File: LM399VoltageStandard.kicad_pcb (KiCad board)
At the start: 2 copper layers, 31 parts, among them J1 Screw_Terminal_01x04, U1 LM399, U2 LT1001, U3 LT3045xDD, U5 LM7815

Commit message: Started PCB
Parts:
- removed D5: 1N4148, Diode_THT:D_DO-35_SOD27_P7.62mm_Horizontal
- added C20: 100n, Capacitor_SMD:C_0603_1608Metric, F.Cu at (143.8, 61.4)
- added C21: 1n, Capacitor_SMD:C_0603_1608Metric, F.Cu at (106.6, 65.1)
- added C22: 10u, Capacitor_Tantalum_SMD:CP_EIA-7132-20_AVX-U, F.Cu at (140.8, 64.2)
- added JP10: Jumper_2_Open, Jumper:SolderJumper-2_P1.3mm_Open_RoundedPad1.0x1.5mm, F.Cu at (124.9, 59.1)
- added JP11: Jumper_2_Open, Jumper:SolderJumper-2_P1.3mm_Open_RoundedPad1.0x1.5mm, F.Cu at (127.4, 59.1)
- added JP12: Jumper_2_Open, Jumper:SolderJumper-2_P1.3mm_Open_RoundedPad1.0x1.5mm, F.Cu at (129.9, 59.1)
- added JP13: Jumper_2_Open, Jumper:SolderJumper-2_P1.3mm_Open_RoundedPad1.0x1.5mm, F.Cu at (132.4, 59.1)
- added JP14: Jumper_2_Open, Jumper:SolderJumper-2_P1.3mm_Open_RoundedPad1.0x1.5mm, F.Cu at (134.9, 59.1)
- added JP8: Jumper_2_Open, Jumper:SolderJumper-2_P1.3mm_Open_RoundedPad1.0x1.5mm, F.Cu at (119.9, 59.1)
- added JP9: Jumper_2_Open, Jumper:SolderJumper-2_P1.3mm_Open_RoundedPad1.0x1.5mm, F.Cu at (122.4, 59.1)
- added R1: 8k06, Resistor_SMD:R_0603_1608Metric, F.Cu at (104.6, 65.0)
- added R10: 8M25, Resistor_THT:R_Axial_DIN0204_L3.6mm_D1.6mm_P7.62mm_Horizontal, F.Cu at (130.1, 61.9)
- added R11: 35k7, Resistor_SMD:R_0603_1608Metric, F.Cu at (117.4, 63.2)
- added R12: 8M25, Resistor_THT:R_Axial_DIN0204_L3.6mm_D1.6mm_P7.62mm_Horizontal, F.Cu at (132.5, 61.9)
- added R13: 511k, Resistor_SMD:R_0603_1608Metric, F.Cu at (119.9, 62.7)
- added R14: 8M25, Resistor_THT:R_Axial_DIN0204_L3.6mm_D1.6mm_P7.62mm_Horizontal, F.Cu at (132.5, 71.9)
- added R15: 32M, Resistor_THT:R_Axial_DIN0207_L6.3mm_D2.5mm_P10.16mm_Horizontal, F.Cu at (135.4, 61.9)
- added R16: 32M, Resistor_SMD:R_0805_2012Metric, F.Cu at (135.4, 65.7)
- added R17: 50R, Resistor_SMD:R_0805_2012Metric, F.Cu at (138.1, 58.4)
- added R4: 5k, LM399VoltageStandard:ZFoilResistor, F.Cu at (114.5, 54.7)
- added R5: 10k, Resistor_THT:R_Axial_DIN0207_L6.3mm_D2.5mm_P10.16mm_Horizontal, F.Cu at (114.5, 61.9)
- added R6: 2k, Resistor_SMD:R_1206_3216Metric, F.Cu at (117.4, 59.2)
- added R7: 1M02, Resistor_SMD:R_0805_2012Metric, F.Cu at (122.4, 62.8)
- added R8: 2M05, Resistor_SMD:R_0805_2012Metric, F.Cu at (124.9, 62.9)
- added R9: 4M12, Resistor_THT:R_Axial_DIN0207_L6.3mm_D2.5mm_P10.16mm_Horizontal, F.Cu at (127.5, 66.3)
- added U4: 7818, Package_TO_SOT_SMD:TO-263-2, F.Cu at (249.8, 117.5)
- moved U1 117.0 mm to (104.4, 72.8), turned to 180 degrees
- moved C6 113.8 mm to (102.9, 65.1), turned to -90 degrees
- moved U2 113.0 mm to (110.4, 63.5), turned to 90 degrees
- moved C1 110.0 mm to (108.9, 59.0), turned to 180 degrees
- moved U5 68.9 mm to (247.7, 100.0)
- moved R3 57.0 mm to (249.1, 128.9)
- moved D6 55.2 mm to (235.3, 108.8)
- moved C14 55.2 mm to (234.8, 121.1)
- moved C9 55.2 mm to (234.8, 114.6)
- moved C18 55.2 mm to (234.8, 127.7)
- moved C10 51.6 mm to (241.1, 139.0)
- moved C7 51.6 mm to (241.1, 134.0)
- moved C8 51.6 mm to (241.1, 136.5)
- moved C2 51.4 mm to (241.1, 131.5)
- moved C11 51.4 mm to (245.1, 128.9)
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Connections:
- C12 pad 2: Masa -> GND_H
- C13 pad 2: Masa -> GND_H
- C14 pad 2: Masa -> GND_H
- C15 pad 2: Masa -> GND_H
- C16 pad 2: Masa -> GND_H
- D6 pad 1: Masa -> GND_H
- U1 pad 4: Masa -> GND_H
- U2 pad 6: /10V -> Net-(JP10-B)
- U5 pad 2: Masa -> GND_H
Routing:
- net Net-(U2--): track 0.00 -> 49.8 mm
- net Net-(JP10-B): track 0.00 -> 28.4 mm
- net Net-(U2-+): track 0.00 -> 16.9 mm
- net Masa: track 0.00 -> 12.6 mm, vias 0 -> 7
- net /10V: track 0.00 -> 7.32 mm
- net Net-(JP11-A): track 0.00 -> 6.57 mm
- net +15V: track 0.00 -> 5.34 mm, vias 0 -> 1
- net Net-(JP14-A): track 0.00 -> 5.19 mm
- net Net-(R12-Pad2): track 0.00 -> 2.47 mm
- net Net-(JP10-A): track 0.00 -> 2.18 mm
- net Net-(JP12-A): track 0.00 -> 2.15 mm
- net Net-(JP9-A): track 0.00 -> 2.12 mm
- net Net-(JP8-A): track 0.00 -> 2.12 mm
- net Net-(JP13-A): track 0.00 -> 2.12 mm
- added copper zone on In1.Cu, net Masa
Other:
- board outline added: 100 x 80 mm
- copper layers 2 -> 4

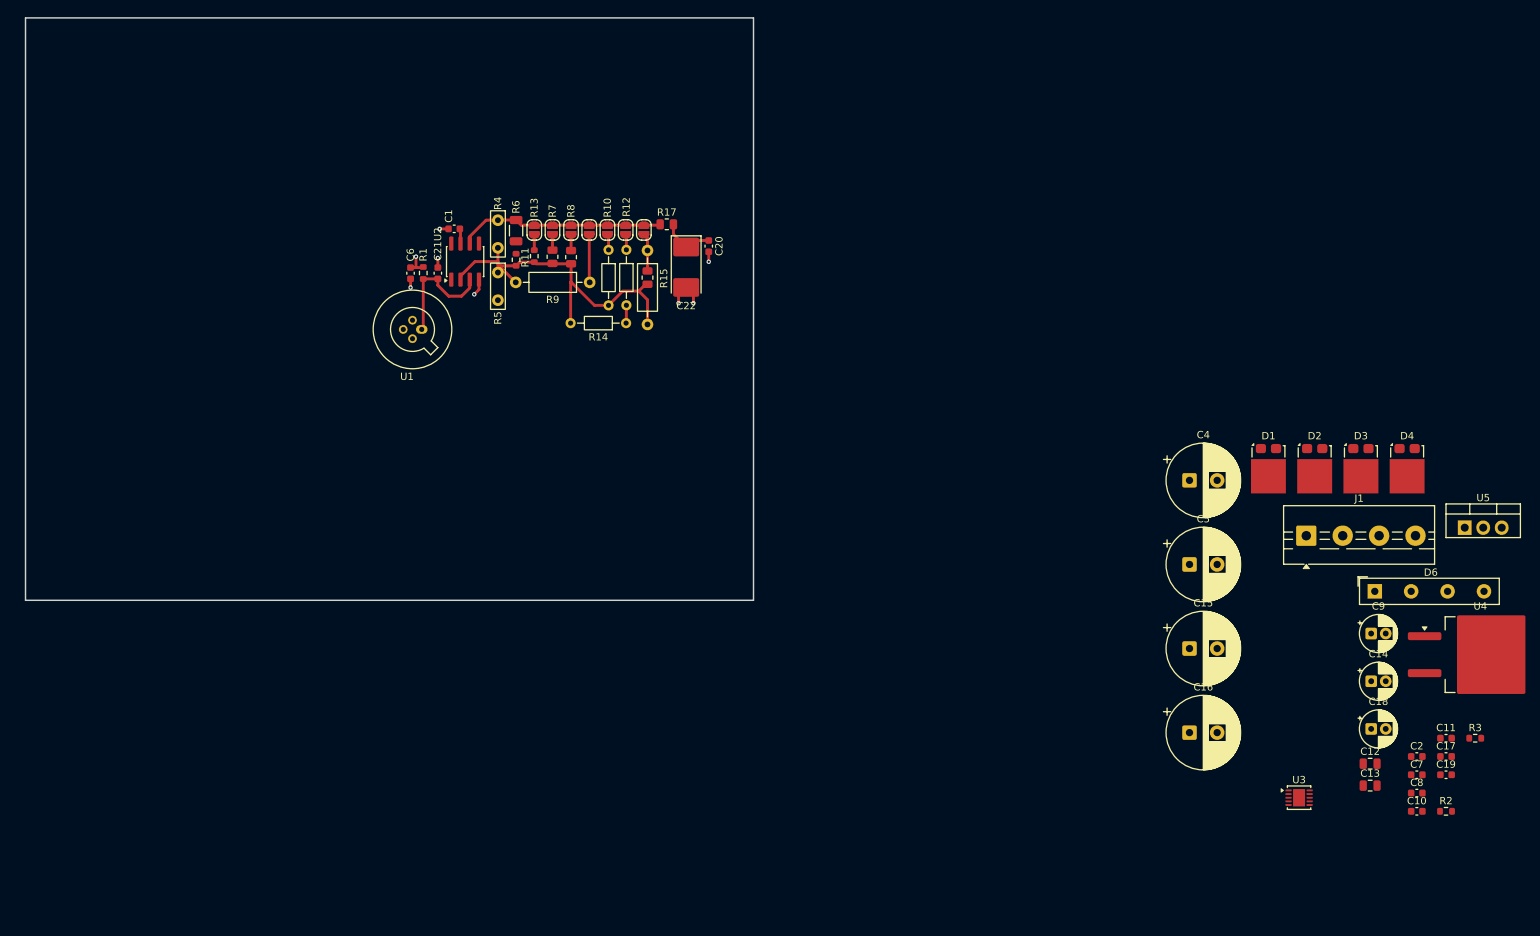
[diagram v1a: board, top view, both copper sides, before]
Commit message: Added MCU
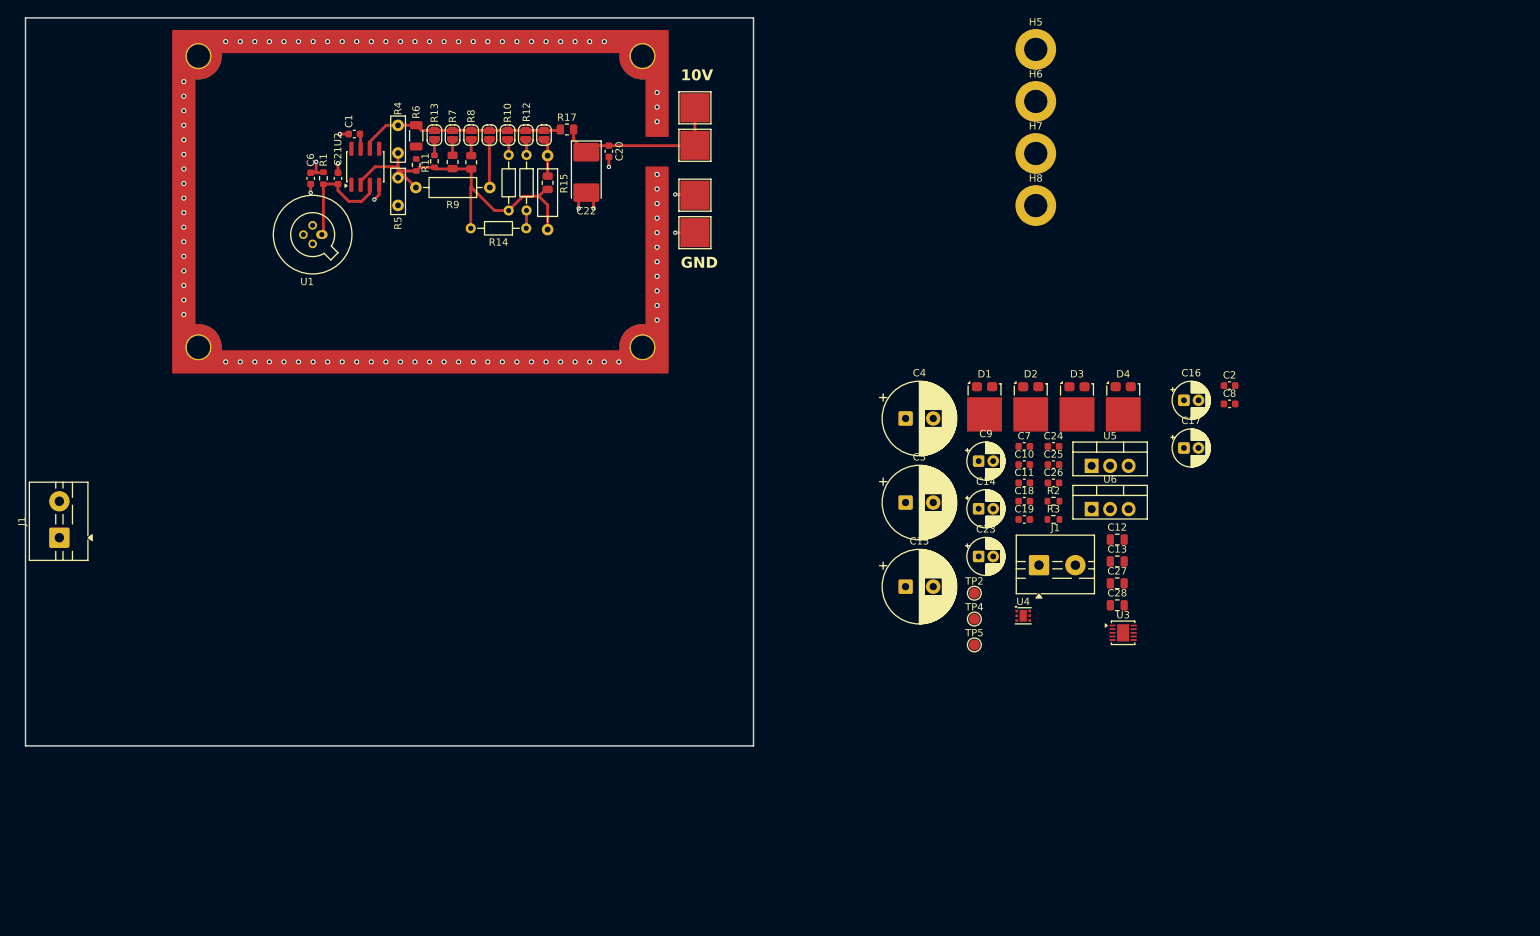
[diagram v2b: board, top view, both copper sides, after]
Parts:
- removed D6: KBP10, Diode_THT:Diode_Bridge_19.0x3.5x10.0mm_P5.0mm
- removed the J1 at (225.9, 101.1)
- added C23: 47u, Capacitor_THT:CP_Radial_D5.0mm_P2.00mm, F.Cu at (180.9, 104.0)
- added C24: 100n, Capacitor_SMD:C_0603_1608Metric, F.Cu at (191.2, 88.9)
- added C25: 100n, Capacitor_SMD:C_0603_1608Metric, F.Cu at (191.2, 91.4)
- added C26: 100n, Capacitor_SMD:C_0603_1608Metric, F.Cu at (191.2, 93.9)
- added C27: 10u, Capacitor_SMD:C_0805_2012Metric, F.Cu at (200.0, 107.7)
- added C28: 10u, Capacitor_SMD:C_0805_2012Metric, F.Cu at (200.0, 110.7)
- added H1: MountingHole_Pad, MountingHole:MountingHole_3.2mm_M3_Pad_TopBottom, F.Cu at (134.8, 75.2)
- added H2: MountingHole_Pad, MountingHole:MountingHole_3.2mm_M3_Pad_TopBottom, F.Cu at (73.8, 75.2)
- added H3: MountingHole_Pad, MountingHole:MountingHole_3.2mm_M3_Pad_TopBottom, F.Cu at (73.8, 35.2)
- added H4: MountingHole_Pad, MountingHole:MountingHole_3.2mm_M3_Pad_TopBottom, F.Cu at (134.8, 35.2)
- added H5: MountingHole, MountingHole:MountingHole_3.2mm_M3_DIN965_Pad, F.Cu at (188.8, 34.3)
- added H6: MountingHole, MountingHole:MountingHole_3.2mm_M3_DIN965_Pad, F.Cu at (188.8, 41.5)
- added H7: MountingHole, MountingHole:MountingHole_3.2mm_M3_DIN965_Pad, F.Cu at (188.8, 48.6)
- added H8: MountingHole, MountingHole:MountingHole_3.2mm_M3_DIN965_Pad, F.Cu at (188.8, 55.8)
- added J1: Screw_Terminal_01x02, TerminalBlock:TerminalBlock_MaiXu_MX126-5.0-02P_1x02_P5.00mm, F.Cu at (189.2, 105.2)
- added J1: Screw_Terminal_01x02, TerminalBlock:TerminalBlock_MaiXu_MX126-5.0-02P_1x02_P5.00mm, F.Cu at (54.6, 101.4)
- added TP2: TestPoint, TestPoint:TestPoint_Pad_D1.5mm, F.Cu at (180.3, 109.0)
- added TP3: TestPoint, TestPoint:TestPoint_Pad_4.0x4.0mm, F.Cu at (141.9, 47.5)
- added TP4: TestPoint, TestPoint:TestPoint_Pad_D1.5mm, F.Cu at (180.3, 112.6)
- added TP5: TestPoint, TestPoint:TestPoint_Pad_D1.5mm, F.Cu at (180.3, 116.1)
- added TP6: TestPoint, TestPoint:TestPoint_Pad_4.0x4.0mm, F.Cu at (141.9, 54.4)
- added TP7: TestPoint, TestPoint:TestPoint_Pad_4.0x4.0mm, F.Cu at (141.9, 42.4)
- added TP8: TestPoint, TestPoint:TestPoint_Pad_4.0x4.0mm, F.Cu at (141.9, 59.5)
- added U6: LM7805_TO220, Package_TO_SOT_THT:TO-220-3_Vertical, F.Cu at (196.4, 97.5)
- C16: value 1000u -> 47u; footprint Capacitor_THT:CP_Radial_D10.0mm_P3.80mm -> Capacitor_THT:CP_Radial_D5.0mm_P2.00mm
- C17: value 100n -> 47u; footprint Capacitor_SMD:C_0603_1608Metric -> Capacitor_THT:CP_Radial_D5.0mm_P2.00mm
- C18: value 47u -> 100n; footprint Capacitor_THT:CP_Radial_D5.0mm_P2.00mm -> Capacitor_SMD:C_0603_1608Metric
- U4: value 7818 -> TLV75533PDRV; footprint Package_TO_SOT_SMD:TO-263-2 -> Package_SON:WSON-6-1EP_2x2mm_P0.65mm_EP1x1.6mm
- moved C10 71.9 mm to (187.2, 91.4)
- moved C7 70.3 mm to (187.2, 88.9)
- moved R2 68.7 mm to (191.2, 96.4)
- moved C11 67.7 mm to (187.2, 93.9)
- moved C19 67.7 mm to (187.2, 98.9)
- moved R3 65.3 mm to (191.2, 98.9)
- moved U4 63.0 mm to (187.0, 112.1)
- moved C8 59.3 mm to (215.4, 83.0)
- moved C14 58.9 mm to (180.9, 97.4)
- moved C9 58.9 mm to (180.9, 90.9)
- moved C2 57.1 mm to (215.4, 80.5)
- moved C18 57.0 mm to (187.2, 96.4)
- moved C17 55.6 mm to (209.1, 89.1)
- moved U5 52.0 mm to (196.4, 91.5)
- moved C13 46.4 mm to (200.0, 104.7)
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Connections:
- C12 pad 1: Net-(D6-+) -> VIN
- C12 pad 2: GND_H -> Masa
- C13 pad 2: GND_H -> Masa
- C14 pad 2: GND_H -> Masa
- C15 pad 1: Net-(D6-+) -> VIN
- C15 pad 2: GND_H -> Masa
- C16 pad 1: Net-(D6-+) -> +15V
- C16 pad 2: GND_H -> Masa
- C17 pad 1: Net-(U3-EN/UV) -> +15V_H
- C18 pad 1: Net-(U3-EN/UV) -> +5V
- C19 pad 1: Net-(U3-EN/UV) -> VIN
- C4 pad 1: Net-(D3-K) -> VIN
- C5 pad 1: Net-(D3-K) -> VIN
- C7 pad 1: Net-(D3-K) -> VIN
- C8 pad 1: Net-(D3-K) -> +15V_H
- D3 pad 3: Net-(D3-K) -> VIN
- D4 pad 3: Net-(D3-K) -> VIN
- U1 pad 4: GND_H -> Masa
- U3 pad 1: Net-(U3-EN/UV) -> VIN
- U3 pad 2: Net-(U3-EN/UV) -> VIN
- U3 pad 3: Net-(U3-EN/UV) -> VIN
- U3 pad 6: Net-(U3-EN/UV) -> VIN
- U4 pad 1: Net-(D3-K) -> +3V3
- U4 pad 2: Masa -> unconnected-(U4-NC-Pad2)
- U4 pad 3: Net-(U3-EN/UV) -> Masa
- U5 pad 1: Net-(D6-+) -> VIN
- U5 pad 2: GND_H -> Masa
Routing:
- net /10V: track 7.32 -> 24.3 mm
- net Masa: track 12.6 -> 18.1 mm, vias 7 -> 95
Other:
- board size 100 x 80 mm -> 100 x 100 mm
- board text added: "10V"
- board text added: "GND"

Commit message: Final Version
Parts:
- removed the J1 at (189.2, 105.2)
- removed the J1 at (54.6, 101.4)
- added C29: 100n, Capacitor_SMD:C_0603_1608Metric, F.Cu at (67.4, 112.5)
- added C30: 100n, Capacitor_SMD:C_0603_1608Metric, F.Cu at (77.5, 114.0)
- added C31: 100n, Capacitor_SMD:C_0603_1608Metric, F.Cu at (68.5, 103.0)
- added C32: 100n, Capacitor_SMD:C_0603_1608Metric, F.Cu at (70.8, 101.5)
- added C33: 100n, Capacitor_SMD:C_0603_1608Metric, F.Cu at (72.5, 101.5)
- added C34: 14p, Capacitor_SMD:C_0603_1608Metric, F.Cu at (83.3, 111.2)
- added C35: 14p, Capacitor_SMD:C_0603_1608Metric, F.Cu at (83.5, 106.9)
- added C36: 100n, Capacitor_SMD:C_0603_1608Metric, F.Cu at (67.2, 125.2)
- added C37: 100n, Capacitor_SMD:C_0603_1608Metric, F.Cu at (62.4, 123.8)
- added C38: 10u, Capacitor_SMD:C_0805_2012Metric, F.Cu at (66.5, 102.8)
- added C39: 2u2, Capacitor_SMD:C_0603_1608Metric, F.Cu at (74.0, 99.5)
- added C40: 100n, Capacitor_SMD:C_0603_1608Metric, F.Cu at (76.0, 115.5)
- added C41: 100n, Capacitor_SMD:C_0603_1608Metric, F.Cu at (76.3, 98.7)
- added C42: 100n, Capacitor_SMD:C_0603_1608Metric, B.Cu at (128.9, 113.5)
- added C43: 100n, Capacitor_SMD:C_0603_1608Metric, B.Cu at (74.1, 107.7)
- added C44: 100n, Capacitor_SMD:C_0603_1608Metric, B.Cu at (76.7, 107.2)
- added C45: 100n, Capacitor_SMD:C_0603_1608Metric, B.Cu at (72.7, 103.6)
- added C46: 100n, Capacitor_SMD:C_0603_1608Metric, B.Cu at (98.3, 68.6)
- added C47: 100n, Capacitor_SMD:C_0603_1608Metric, B.Cu at (64.9, 105.4)
- added D5: LED_BGKR, LED_THT:LED_D5.0mm-4_RGB_Wide_Pins, F.Cu at (83.5, 96.4)
- added FB1: 120R, Inductor_SMD:L_0603_1608Metric, F.Cu at (76.3, 100.3)
- added J1: Screw_Terminal_01x02, TerminalBlock:TerminalBlock_MaiXu_MX126-5.0-02P_1x02_P5.00mm, F.Cu at (100.8, 125.8)
- added J2: USB_B_Micro, Connector_USB:USB_Micro-B_Technik_TWP-4002D-H3, F.Cu at (55.2, 108.0)
- added J3: Conn_01x04, Connector_PinHeader_2.54mm:PinHeader_1x04_P2.54mm_Vertical, F.Cu at (57.9, 116.5)
- added J4: Conn_01x02, Connector_PinHeader_2.54mm:PinHeader_1x02_P2.54mm_Vertical, F.Cu at (88.8, 106.1)
- added JP15: Jumper_2_Open, Jumper:SolderJumper-2_P1.3mm_Open_RoundedPad1.0x1.5mm, B.Cu at (140.8, 34.0)
- added JP16: Jumper_2_Open, Jumper:SolderJumper-2_P1.3mm_Open_RoundedPad1.0x1.5mm, B.Cu at (146.2, 121.2)
- added JP17: Jumper_2_Open, Jumper:SolderJumper-2_P1.3mm_Open_RoundedPad1.0x1.5mm, B.Cu at (54.0, 120.8)
- added JP18: Jumper_2_Open, Jumper:SolderJumper-2_P1.3mm_Open_RoundedPad1.0x1.5mm, B.Cu at (54.0, 39.4)
- added R18: 10k, Resistor_SMD:R_0603_1608Metric, F.Cu at (60.2, 102.8)
- added R19: 10k, Resistor_SMD:R_0603_1608Metric, F.Cu at (63.3, 102.8)
- added R20: 1k5, Resistor_SMD:R_0603_1608Metric, F.Cu at (62.0, 111.2)
- added R21: 4k7, Resistor_SMD:R_0603_1608Metric, F.Cu at (73.5, 116.4)
- added R22: 4k7, Resistor_SMD:R_0603_1608Metric, F.Cu at (70.0, 115.8)
- added R23: 0R1, Resistor_SMD:R_0805_2012Metric, B.Cu at (135.9, 120.6)
- added R24: 4k, Resistor_SMD:R_0603_1608Metric, F.Cu at (109.0, 103.2)
- added R25: 20k, Resistor_SMD:R_0603_1608Metric, F.Cu at (109.0, 105.0)
- added R26: 20k, Resistor_SMD:R_0603_1608Metric, B.Cu at (102.5, 102.3)
- added R27: 4k, Resistor_SMD:R_0603_1608Metric, B.Cu at (104.9, 103.2)
- added R28: 100R, Resistor_SMD:R_0603_1608Metric, B.Cu at (66.3, 103.1)
- added U10: TMP102xxDRL, Package_TO_SOT_SMD:SOT-563, F.Cu at (61.9, 126.6)
- added U11: INA180B3, Package_TO_SOT_SMD:SOT-23-5, B.Cu at (132.2, 115.5)
- added U12: LM35-LP, Package_TO_SOT_THT:TO-92_Inline, F.Cu at (96.9, 70.7)
- added U7: STM32G431C6Tx, Package_QFP:LQFP-48_7x7mm_P0.5mm, F.Cu at (72.8, 108.5)
- added U8: USBLC6-2SC6, Package_TO_SOT_SMD:SOT-23-6, F.Cu at (60.9, 107.8)
- added U9: FM24C64B, Package_SO:SOIC-8_3.9x4.9mm_P1.27mm, F.Cu at (68.8, 121.8)
- added Y1: Crystal_GND24, Crystal:Crystal_SMD_EuroQuartz_X22-4Pin_2.5x2.0mm_HandSoldering, F.Cu at (81.2, 109.2)
- C12, C13, C25, C7, C8: moved to B.Cu
- H5, H6, H7, H8: value MountingHole -> MountingHole_Pad; footprint MountingHole:MountingHole_3.2mm_M3_DIN965_Pad -> MountingHole:MountingHole_3.2mm_M3_Pad_TopBottom
- moved H7 155.4 mm to (54.0, 126.0)
- moved H8 136.5 mm to (54.0, 34.0)
- moved C8 129.7 mm to (87.5, 61.8), turned to -45 degrees
- moved C17 128.6 mm to (82.2, 68.4), turned to 180 degrees
- moved C2 126.8 mm to (93.8, 44.3), turned to 180 degrees
- moved C28 119.0 mm to (81.5, 122.1)
- moved C24 117.7 mm to (77.9, 120.8), turned to 180 degrees
- moved C27 115.9 mm to (84.7, 119.5), turned to -90 degrees
- moved U6 114.9 mm to (85.3, 126.7), turned to 180 degrees
- moved C26 111.4 mm to (82.8, 119.3), turned to -90 degrees
- moved C16 110.7 mm to (100.5, 61.5), turned to -90 degrees
- moved C18 109.3 mm to (81.5, 124.2)
- moved C25 107.4 mm to (89.5, 125.9), turned to -90 degrees
- moved U4 106.8 mm to (80.5, 118.7), turned to -90 degrees
- moved D3 104.3 mm to (95.0, 115.0), turned to 180 degrees
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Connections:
- C12 pad 1: VIN -> /PowerSupply/HEATER_SENSE_L
- C15 pad 1: VIN -> /PowerSupply/HEATER_SENSE_L
- H5 pad 1: (no net) -> Net-(JP15-A)
- H6 pad 1: (no net) -> Net-(JP16-A)
- H7 pad 1: (no net) -> Net-(JP17-A)
- H8 pad 1: (no net) -> Net-(JP18-A)
- U5 pad 1: VIN -> /PowerSupply/HEATER_SENSE_L
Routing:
- net +15V_H: track 0.00 -> 129.4 mm, vias 0 -> 1
- net Masa: track 18.1 -> 113.6 mm, vias 95 -> 144
- net +3V3: track 0.00 -> 81.1 mm, vias 0 -> 11
- net HEATER_SENSE_OUT: track 0.00 -> 64.2 mm, vias 0 -> 1
- net +15V: track 5.34 -> 63.8 mm, vias 1 -> 4
- net TEMP_SENSE: track 0.00 -> 46.7 mm, vias 0 -> 2
- net VIN: track 0.00 -> 42.6 mm, vias 0 -> 2
- net REFERENCE_VOLTAGE_SENSE: track 0.00 -> 38.3 mm, vias 0 -> 1
- net HEATER_VOLTAGE_SENSE: track 0.00 -> 34.8 mm, vias 0 -> 1
- net /MCU/SCL1: track 0.00 -> 23.5 mm
- net /MCU/SDA1: track 0.00 -> 22.7 mm, vias 0 -> 3
- net /PowerSupply/HEATER_SENSE_L: track 0.00 -> 21.9 mm, vias 0 -> 2
- net Net-(D2-K): track 0.00 -> 17.1 mm
- net Net-(D1-K): track 0.00 -> 17.1 mm
- net /MCU/LED_B: track 0.00 -> 13.3 mm
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- added copper zone on In2.Cu, net +15V
- added copper zone on In2.Cu, net +3V3
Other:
- board text added: "+3V3"
- board text added: "0"
- board text added: "1"
- board text added: "2"
- board text added: "3"
- board text added: "4"
- board text added: "5"
- board text added: "6"
- board text added: "Binary Trim Network"
- board text added: "CAL_EN"
- board text added: "Date:"
- board text added: "Initial Voltage:"
- board text added: "LM399"
- board text added: "LM399 S/N"
- board text added: "LM399 Voltage Standard"
- board text added: "Rev 1"
- board text added: "SWCLK"
- board text added: "SWDIO"
- board text added: "Temperature:"

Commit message: Silkscreen fix
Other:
- board text added: "Heater +15V"
- board text added: "Reference +15V"
